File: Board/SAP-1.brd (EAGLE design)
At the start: 135 x 300 mm, 305 parts, among them J1 TERMINAL-1BRIDGE, J2 TERMINAL-1BRIDGE

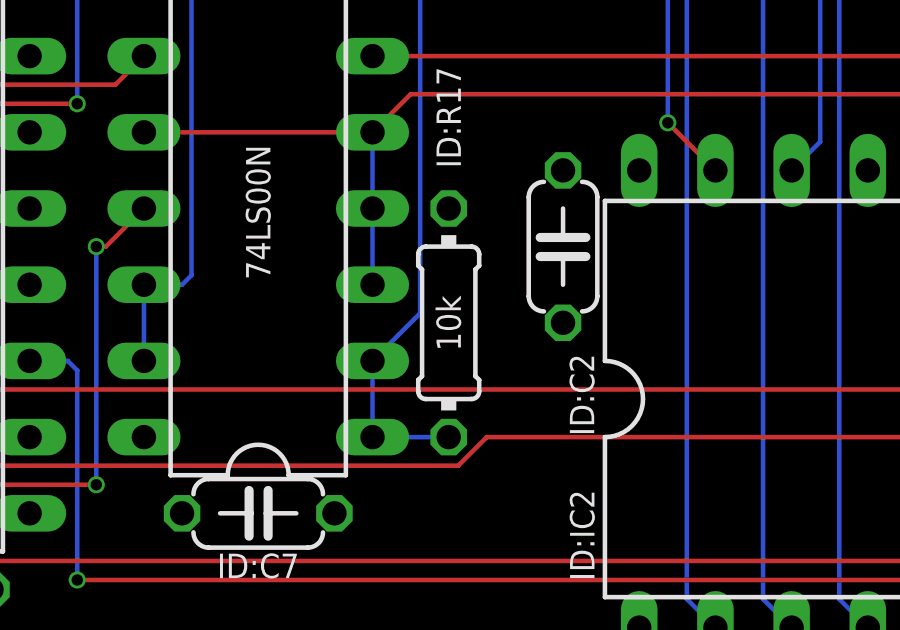
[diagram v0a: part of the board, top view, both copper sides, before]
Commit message: lowered value of reset pull down
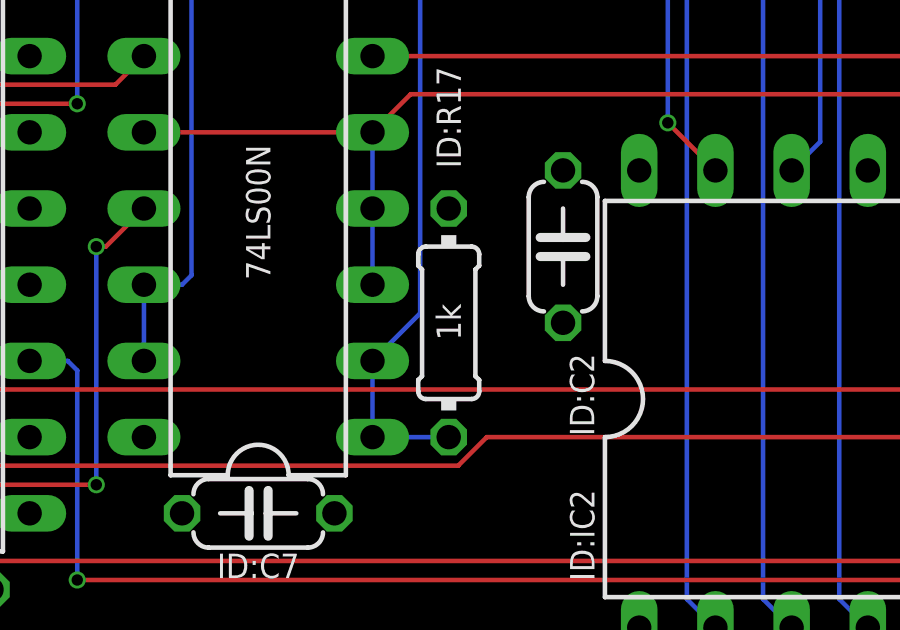
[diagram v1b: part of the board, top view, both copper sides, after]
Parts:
- ID:R17: value 10k -> 1k
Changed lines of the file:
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@@
 <attribute name="SF_SKU" value="COM-09190" x="-1228.14" y="42.21" size="1.778" layer="27" rot="R270" display="off"/>
 </element>
-<element name="ID:R17" library="rcl" library_urn="urn:adsk.eagle:library:334" package="0204/7" package3d_urn="urn:adsk.eagle:package:23498/2" value="10k" x="36.83" y="20.32" smashed="yes" rot="R270">
-<attribute name="MOUSER" value="594-5063JD10K00F" x="-1228.22" y="19.81" size="1.778" layer="27" rot="R270" display="off"/>
+<element name="ID:R17" library="rcl" library_urn="urn:adsk.eagle:library:334" package="0204/7" package3d_urn="urn:adsk.eagle:package:23498/2" value="1k" x="36.83" y="20.32" smashed="yes" rot="R270">
+<attribute name="MOUSER" value="594-5063JD1K000F" x="-1228.22" y="19.81" size="1.778" layer="27" rot="R270" display="off"/>
 <attribute name="NAME" x="36.83" y="25.4762" size="0.8128" layer="25" font="vector" ratio="10" rot="R90" align="center-left"/>
 <attribute name="SPICEPREFIX" value="R" x="-1228.22" y="19.81" size="1.778" layer="27" rot="R270" display="off"/>
-<attribute name="VALUE" x="36.83" y="19.373715625" size="0.8128" layer="25" font="vector" ratio="10" rot="R90" align="center-left"/>
+<attribute name="VALUE" x="36.83" y="19.739475" size="0.8128" layer="25" font="vector" ratio="10" rot="R90" align="center-left"/>
 </element>
 <element name="ID:IC7" library="74xx-us" library_urn="urn:adsk.eagle:library:88" package="DIL14" package3d_urn="urn:adsk.eagle:package:16407/2" value="74LS00N" x="30.48" y="24.13" smashed="yes" rot="R90">

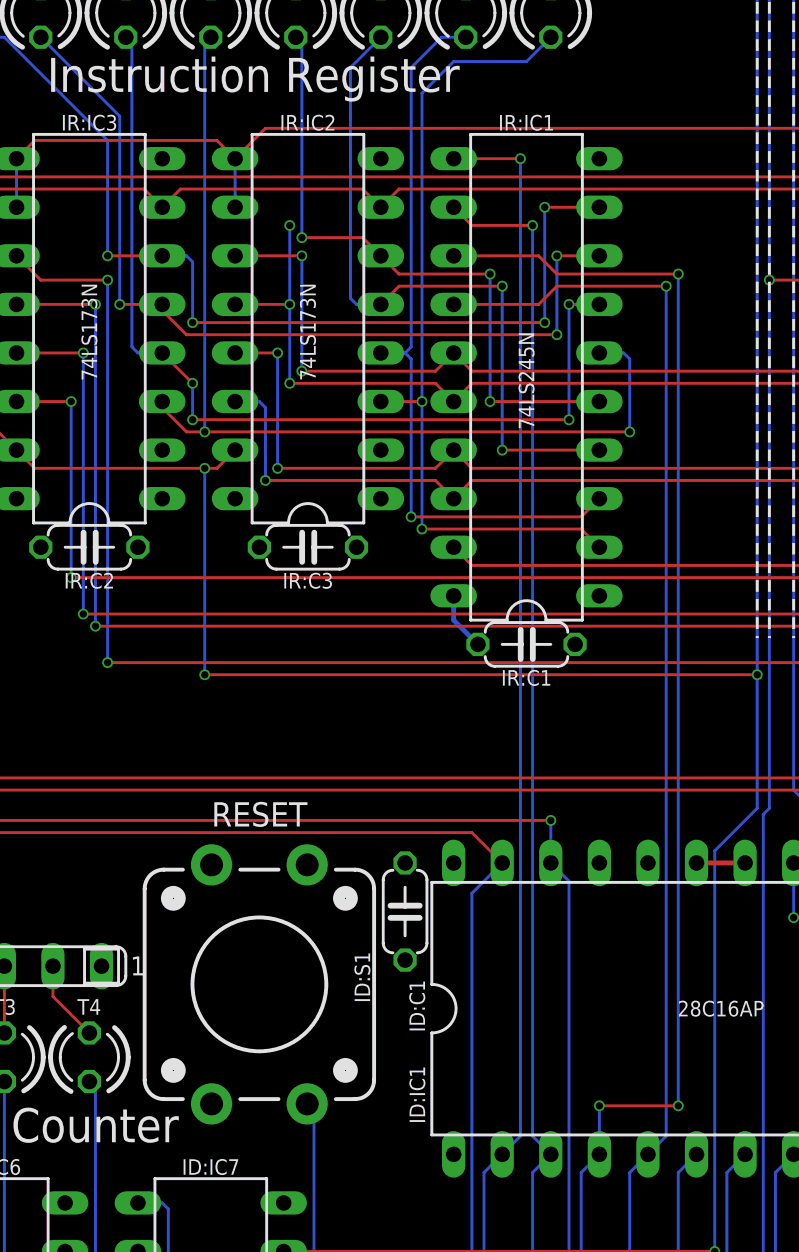
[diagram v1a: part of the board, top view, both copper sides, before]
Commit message: removed buffering of instruction register upper nibble
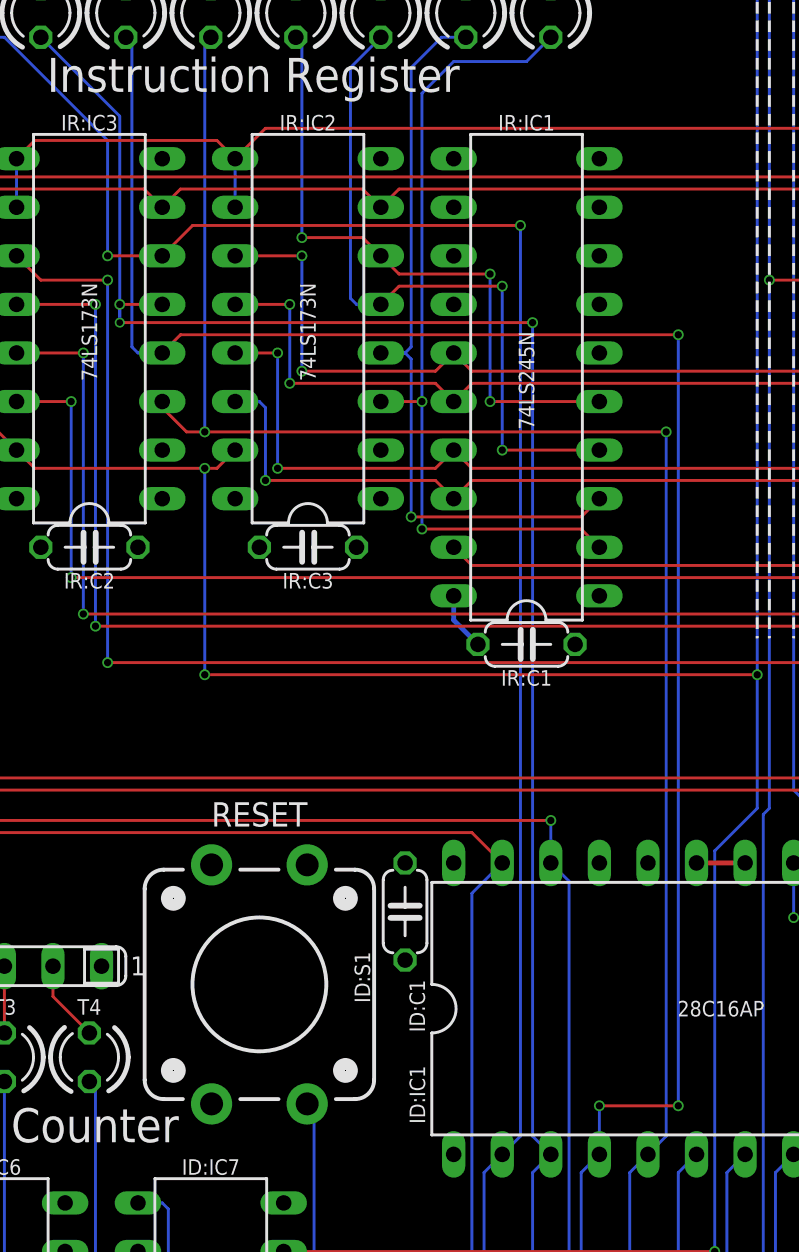
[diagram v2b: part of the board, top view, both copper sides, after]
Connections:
- removed net IR:B5: IR:IC1.6, IR:IC3.3, IR:LED5.A
- removed net IR:B6: IR:IC1.7, IR:IC3.4, IR:LED6.A
- removed net IR:B7: IR:IC1.8, IR:IC3.5, IR:LED7.A
- removed net IR:B8: IR:IC1.9, IR:IC3.6, IR:LED8.A
- net GND: now also IR:IC1.6, IR:IC1.7, IR:IC1.8, IR:IC1.9
- net N$31: now also IR:IC3.3, IR:LED5.A; no longer IR:IC1.14
- net N$33: now also IR:IC3.4, IR:LED6.A; no longer IR:IC1.13
- net N$34: now also IR:IC3.5, IR:LED7.A; no longer IR:IC1.12
- net N$35: now also IR:IC3.6, IR:LED8.A; no longer IR:IC1.11
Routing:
- net IR:B5: track 51.6 -> 0.00 mm, vias 2 -> 0
- net IR:B8: track 51.3 -> 0.00 mm, vias 4 -> 0
- net IR:B6: track 49.5 -> 0.00 mm, vias 4 -> 0
- net IR:B7: track 45.7 -> 0.00 mm, vias 3 -> 0
- net N$34: track 78.4 -> 110.2 mm, vias 1 -> 3
- net N$35: track 80.9 -> 112.3 mm, vias 1 -> 2
- net N$33: track 87.2 -> 117.3 mm
- net N$31: track 82.2 -> 111.1 mm, vias 1 -> 2
- net D3: track 568.1 -> 564.0 mm, vias 21 -> 20

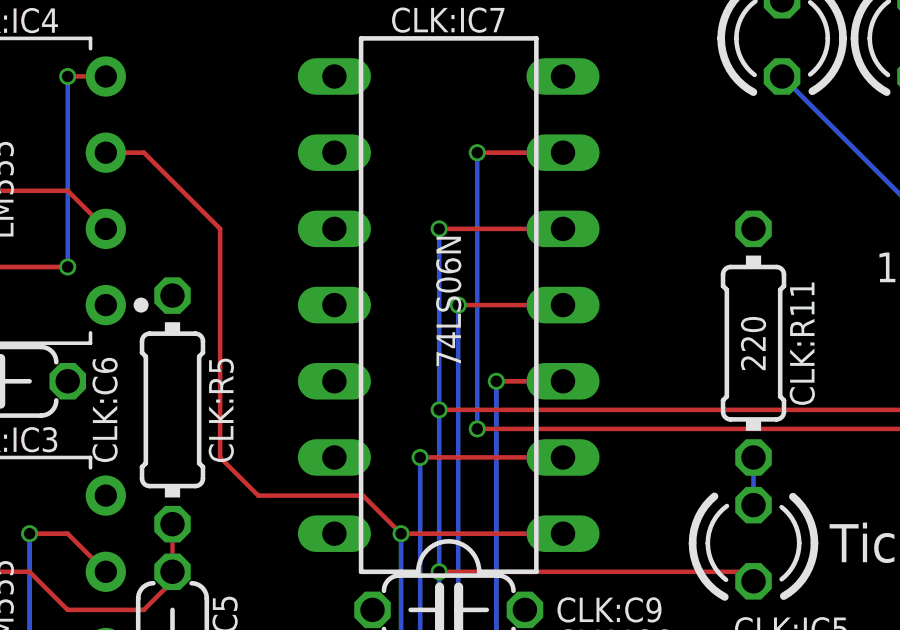
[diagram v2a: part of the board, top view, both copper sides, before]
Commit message: fixed partnumber of CLK:IC7 (74LS06->74LLS04) to fix #1
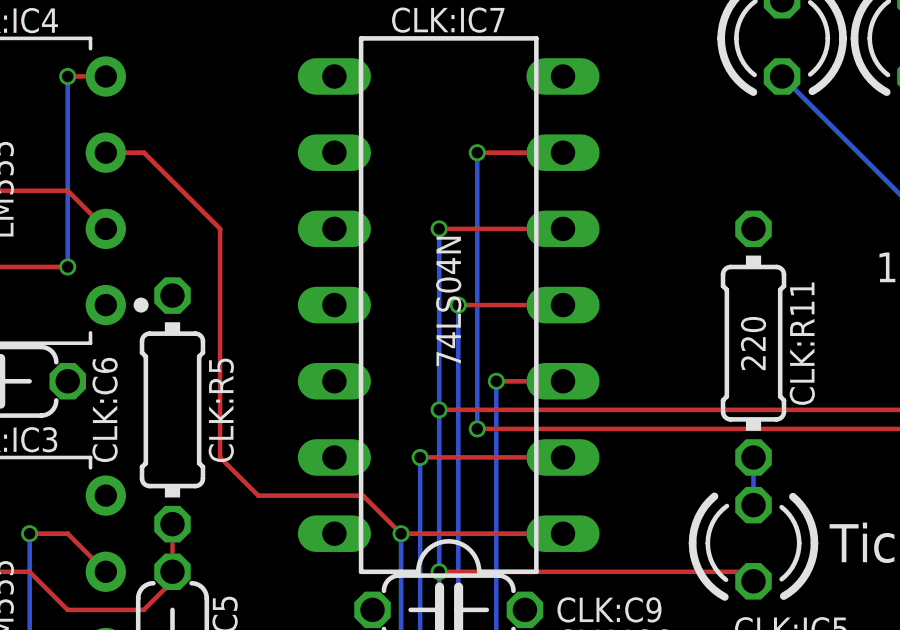
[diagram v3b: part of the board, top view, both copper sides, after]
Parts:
- CLK:IC7: value 74LS06N -> 74LS04N
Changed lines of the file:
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@@
 <?xml version="1.0" encoding="utf-8"?>
 <!DOCTYPE eagle SYSTEM "eagle.dtd">
-<eagle version="9.4.1">
+<eagle version="9.5.1">
 <drawing>
 <settings>
@@
 <setting verticaltext="up"/>
 </settings>
-<grid distance="50" unitdist="mil" unit="mil" style="lines" multiple="1" display="yes" altdistance="12.5" altunitdist="mil" altunit="mil"/>
+<grid distance="1" unitdist="mm" unit="mm" style="lines" multiple="1" display="yes" altdistance="0.5" altunitdist="mm" altunit="mm"/>
 <layers>
 <layer number="1" name="Top" color="4" fill="1" visible="yes" active="yes"/>
@@
 <attribute name="VALUE" x="40.64" y="265.2663125" size="0.8128" layer="25" font="vector" ratio="10" rot="R270" align="center-left"/>
 </element>
-<element name="CLK:IC7" library="74xx-us" library_urn="urn:adsk.eagle:library:88" package="DIL14" package3d_urn="urn:adsk.eagle:package:16407/2" value="74LS06N" x="40.64" y="283.21" smashed="yes" rot="R90">
-<attribute name="MOUSER" value="595-SN74LS06N" x="40.56" y="282.26" size="1.778" layer="27" rot="R90" display="off"/>
+<element name="CLK:IC7" library="74xx-us" library_urn="urn:adsk.eagle:library:88" package="DIL14" package3d_urn="urn:adsk.eagle:package:16407/2" value="74LS04N" x="40.64" y="283.21" smashed="yes" rot="R90">
+<attribute name="MOUSER" value="595-SN74LS04N" x="40.56" y="282.26" size="1.778" layer="27" rot="R90" display="off"/>
 <attribute name="NAME" x="40.64" y="292.3032" size="0.8128" layer="25" font="vector" ratio="10" align="bottom-center"/>
 <attribute name="VALUE" x="40.64" y="285.5863125" size="0.8128" layer="25" font="vector" ratio="10" rot="R270" align="center-left"/>
